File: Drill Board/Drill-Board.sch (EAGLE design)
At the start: 37 parts, among them J1 SL03THROUGH_HOLE, J2 SL03THROUGH_HOLE, J3 APP_2POS_CONFIG5V_HORIZ, J4 SL02-HORIZ, J6 SL03THROUGH_HOLE, U1 OKI-78SR-5/1.5-W36HC

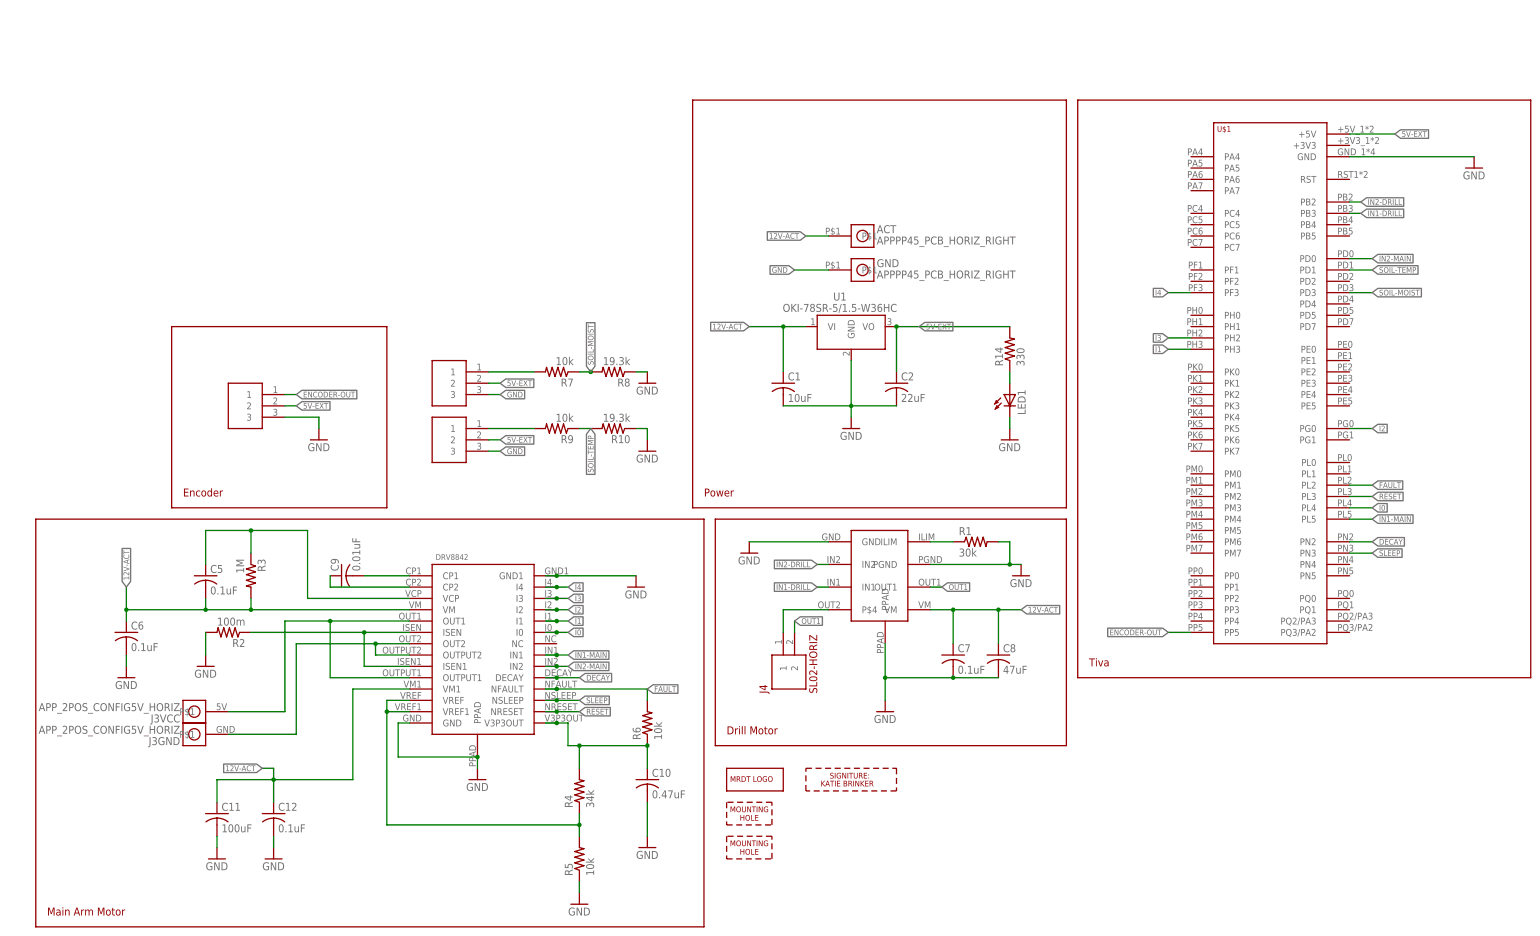
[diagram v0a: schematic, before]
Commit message: Drill Board: Starting from a clean slate (power and filtering only)
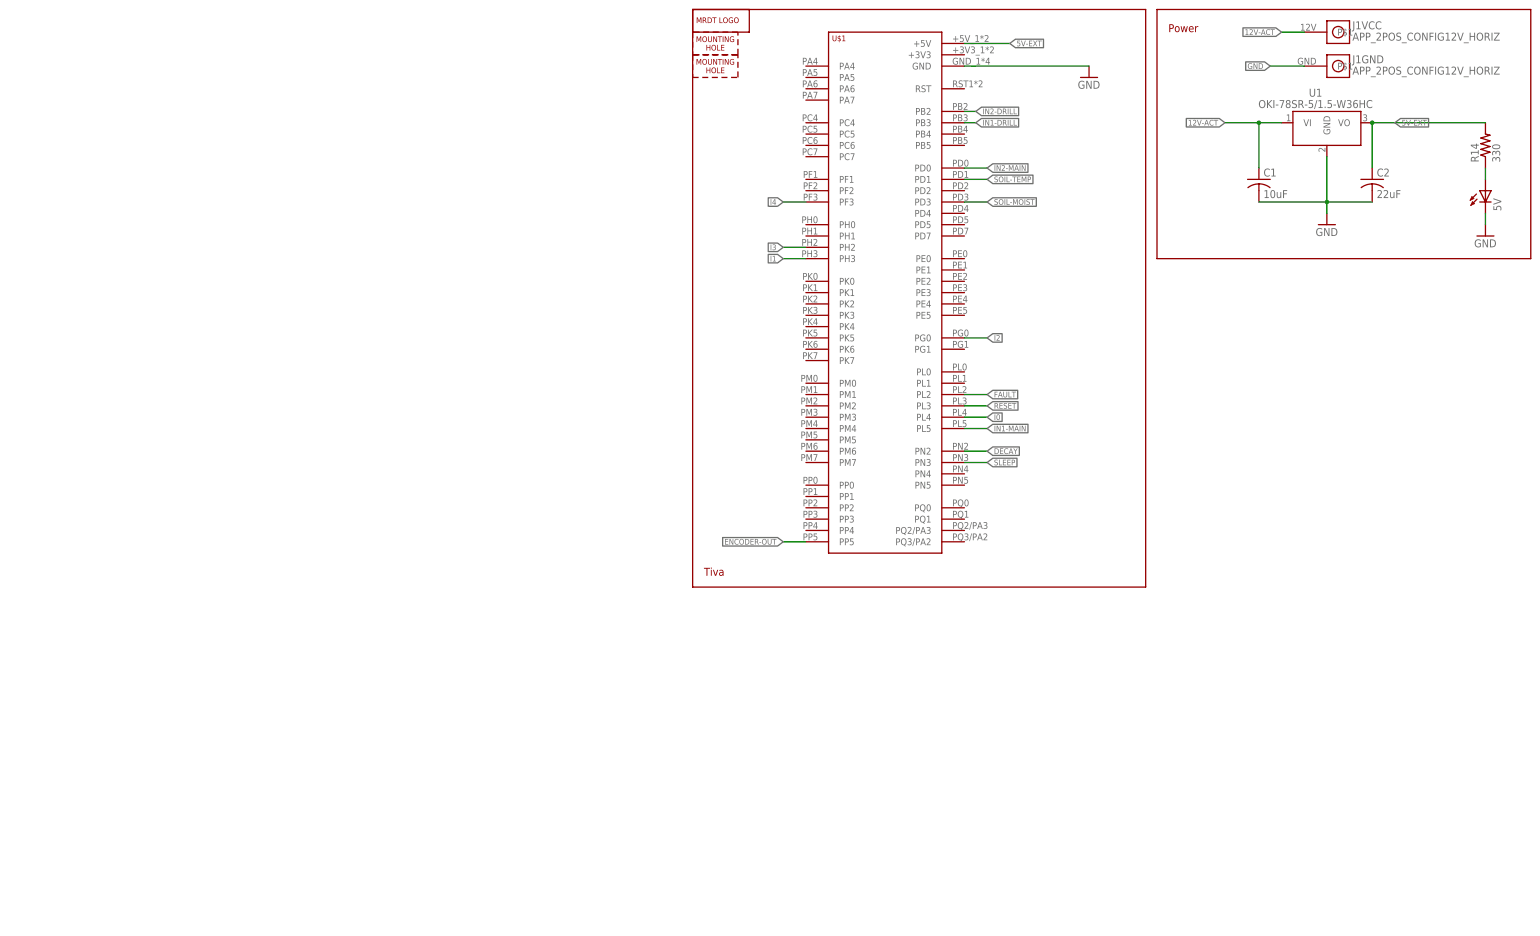
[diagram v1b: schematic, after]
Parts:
- removed ACT, GND: APPPP45_PCB_HORIZ_RIGHT, MRDT-Connectors:APPPP45_PCB_HORIZ_RIGHT
- removed C10: 0.47uF, rcl:C-USC0805
- removed C11: 100uF, rcl:C-USC0805
- removed C12, C5, C6, C7: 0.1uF, rcl:C-USC0805
- removed C8: 47uF, rcl:C-USC0805
- removed C9: 0.01uF, rcl:C-USC0805
- removed J2, J6: SL03THROUGH_HOLE, MRDT-Connectors:SL03THROUGH_HOLE
- removed J3: APP_2POS_CONFIG5V_HORIZ, MRDT-Connectors:APP_2POS_CONFIG5V_HORIZ
- removed J4: SL02-HORIZ, MRDT-Connectors:SL02-HORIZ
- removed LED1: (no value), led:LEDCHIP-LED0805
- removed R1: 30k, rcl:R-US_R0805
- removed R10, R8: 19.3k, rcl:R-US_R0805
- removed R2: 100m, rcl:R-US_R0805
- removed R3: 1M, rcl:R-US_R0805
- removed R4: 34k, rcl:R-US_R0805
- removed R5, R6, R7, R9: 10k, rcl:R-US_R0805
- removed U$2: DRV8842, DRV8842:DRV8842
- removed U$3: DRV8871, drill-motor-driver:DRV8871
- removed U$5: KATIE-BRINKER, sig:KATIE-BRINKER
- added 5V: (no value), led:LEDCHIP-LED0805
- J1: value SL03THROUGH_HOLE -> APP_2POS_CONFIG12V_HORIZ; device MRDT-Connectors:SL03THROUGH_HOLE -> MRDT-Connectors:APP_2POS_CONFIG12V_HORIZ
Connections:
- removed net 3V3: C10.1, R4.2, R6.1, U$2.V3P3OUT
- removed net N$1: R1.1, U$3.ILIM
- removed net N$2: J4.1, U$3.P$4
- removed net N$3: R2.1, U$2.ISEN, U$2.ISEN1
- removed net N$35: J1.1, R7.2
- removed net N$36: J2.1, R9.2
- removed net N$6: C9.2, U$2.CP1
- removed net N$7: C9.1, U$2.CP2
- removed net N$8: C5.1, R3.1, U$2.VCP
- removed net N$9: R4.1, R5.2, U$2.VREF, U$2.VREF1
- removed net OUT1: J4.2, U$3.OUT1
- removed net OUTPUT1: J3VCC.P$1, U$2.OUT1, U$2.OUTPUT1
- removed net OUTPUT2: J3GND.P$1, U$2.OUT2, U$2.OUTPUT2
- net 12V-ACT: now also J1VCC.P$1; no longer ACT.P$1, C11.1, C12.1, C5.2, C6.1, C7.1, C8.1, R3.2, U$2.VM, U$2.VM1, U$3.VM
- net 5V-EXT: no longer J1.2, J2.2, J6.2
- net DECAY: no longer U$2.DECAY
- net ENCODER-OUT: no longer J6.1
- net FAULT: no longer R6.2, U$2.NFAULT
- net GND: now also 5V.C, J1GND.P$1; no longer C10.2, C11.2, C12.2, C6.2, C7.2, C8.2, GND.P$1, J1.3, J2.3, J6.3, LED1.C, R1.2, R10.1, R2.2, R5.1, R8.1, U$2.GND, U$2.GND1, U$2.PPAD, U$3.GND, U$3.PGND, U$3.PPAD
- net I0: no longer U$2.I0
- net I1: no longer U$2.I1
- net I2: no longer U$2.I2
- net I3: no longer U$2.I3
- net I4: no longer U$2.I4
- net IN1-DRILL: no longer U$3.IN1
- net IN1-MAIN: no longer U$2.IN1
- net IN2-DRILL: no longer U$3.IN2
- net IN2-MAIN: no longer U$2.IN2
- net N$37: now also 5V.A; no longer LED1.A
- net RESET: no longer U$2.NRESET
- net SLEEP: no longer U$2.NSLEEP
- net SOIL-MOIST: no longer R7.1, R8.2
- net SOIL-TEMP: no longer R10.2, R9.1
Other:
- note removed: "Drill Motor"
- note removed: "Encoder"
- note removed: "Main Arm Motor"
- moved on the sheet: C1, C2, R14, U$1, U1
